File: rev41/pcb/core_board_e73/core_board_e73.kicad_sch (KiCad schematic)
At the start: 17 parts, among them J1 USB_C_Receptacle_USB2.0_16P, J2 Conn_02x10_Odd_Even, J3 Conn_02x10_Odd_Even, J4 USB_C_Receptacle_USB2.0_16P, J5 Conn_01x08_MountingPin, J6 Conn_01x08_MountingPin, J7 Debug, U1 E73-2G4M08S1C, Y1 32.768kHz

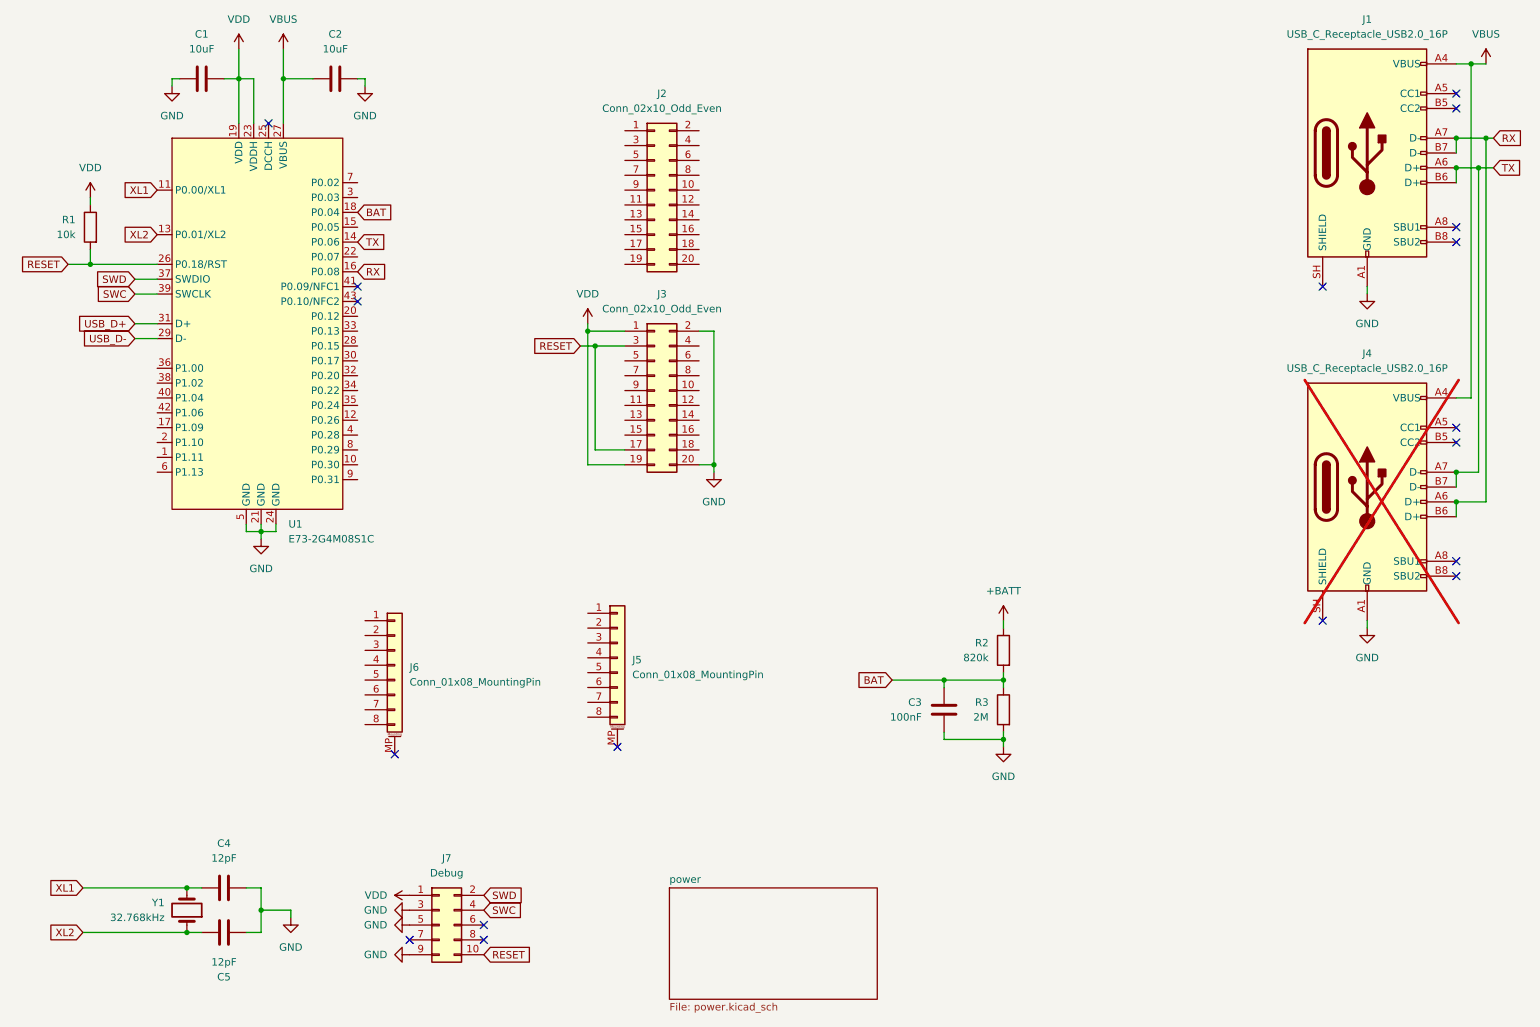
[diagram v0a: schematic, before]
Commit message: feat: core board e73 basic routed
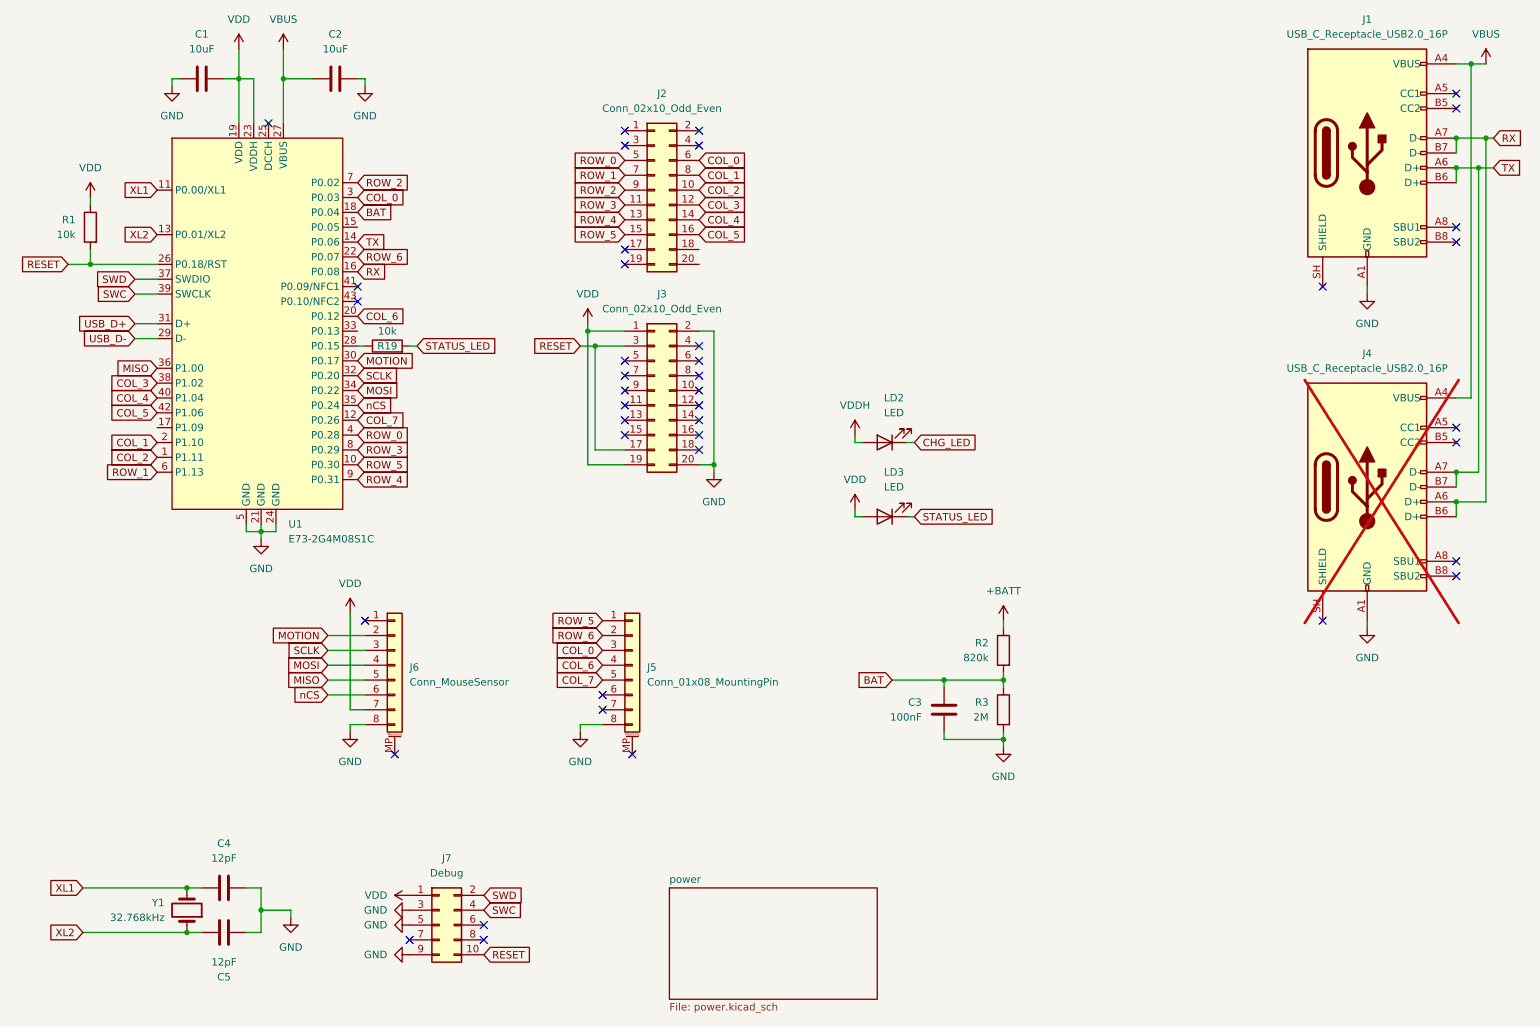
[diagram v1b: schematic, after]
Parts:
- added LD2, LD3: LED, LED_SMD:LED_0603_1608Metric_Pad1.05x0.95mm_HandSolder, symbol Device:LED
- added R19: 10k, Resistor_SMD:R_0402_1005Metric, symbol Device:R
- J6: value Conn_01x08_MountingPin -> Conn_MouseSensor
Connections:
- net GND: now also J5.8 (Pin_8), J6.8 (Pin_8)
- net VDD: now also J6.7 (Pin_7), LD3.2 (A)
- net MOTION: now reaches J6.2 (Pin_2)
- net MOTION: now also U1.30 (P0.17)
- net SCLK: now reaches J6.3 (Pin_3)
- net SCLK: now also U1.32 (P0.20)
- net MOSI: now reaches J6.4 (Pin_4)
- net MOSI: now also U1.34 (P0.22)
- net MISO: now reaches J6.5 (Pin_5)
- net MISO: now also U1.36 (P1.00)
- net nCS: now reaches J6.6 (Pin_6)
- net nCS: now also U1.35 (P0.24)
- net COL_2: now reaches J2.10 (Pin_10)
- net COL_2: now also U1.1 (P1.11)
- net ROW_3: now reaches J2.11 (Pin_11)
- net ROW_3: now also U1.8 (P0.29)
- net COL_3: now reaches J2.12 (Pin_12)
- net COL_3: now also U1.38 (P1.02)
- net ROW_4: now reaches J2.13 (Pin_13)
- net ROW_4: now also U1.9 (P0.31)
- net COL_4: now reaches J2.14 (Pin_14)
- net COL_4: now also U1.40 (P1.04)
- net ROW_5: now reaches J2.15 (Pin_15)
- net ROW_5: now also J5.1 (Pin_1), U1.10 (P0.30)
- net COL_5: now reaches J2.16 (Pin_16)
- net COL_5: now also U1.42 (P1.06)
- net ROW_0: now reaches J2.5 (Pin_5)
- net ROW_0: now also U1.4 (P0.28)
- net COL_0: now reaches J2.6 (Pin_6)
- net COL_0: now also J5.3 (Pin_3), U1.3 (P0.03)
- net ROW_1: now reaches J2.7 (Pin_7)
- net ROW_1: now also U1.6 (P1.13)
- net COL_1: now reaches J2.8 (Pin_8)
- net COL_1: now also U1.2 (P1.10)
- net ROW_2: now reaches J2.9 (Pin_9)
- net ROW_2: now also U1.7 (P0.02)
- net COL_7: now reaches U1.12 (P0.26)
- net COL_7: now also J5.5 (Pin_5)
- net COL_6: now reaches U1.20 (P0.12)
- net COL_6: now also J5.4 (Pin_4)
- net ROW_6: now reaches U1.22 (P0.07)
- net ROW_6: now also J5.2 (Pin_2)
- net at U1.28 (P0.15): now also R19.1
- new net CHG_LED: LD2.1 (K)
- new net STATUS_LED: LD3.1 (K), R19.2
- new net VDDH: LD2.2 (A)
- no-connect marks 18 -> 41
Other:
- moved on the sheet: J5

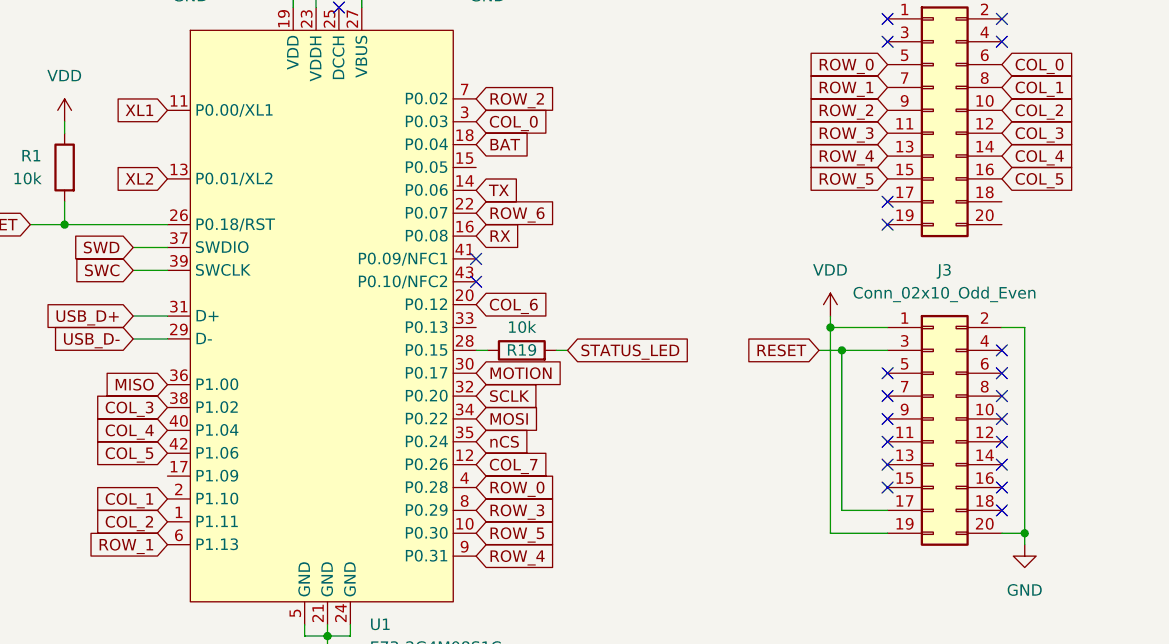
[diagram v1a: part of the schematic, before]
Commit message: feat: update silkscreen
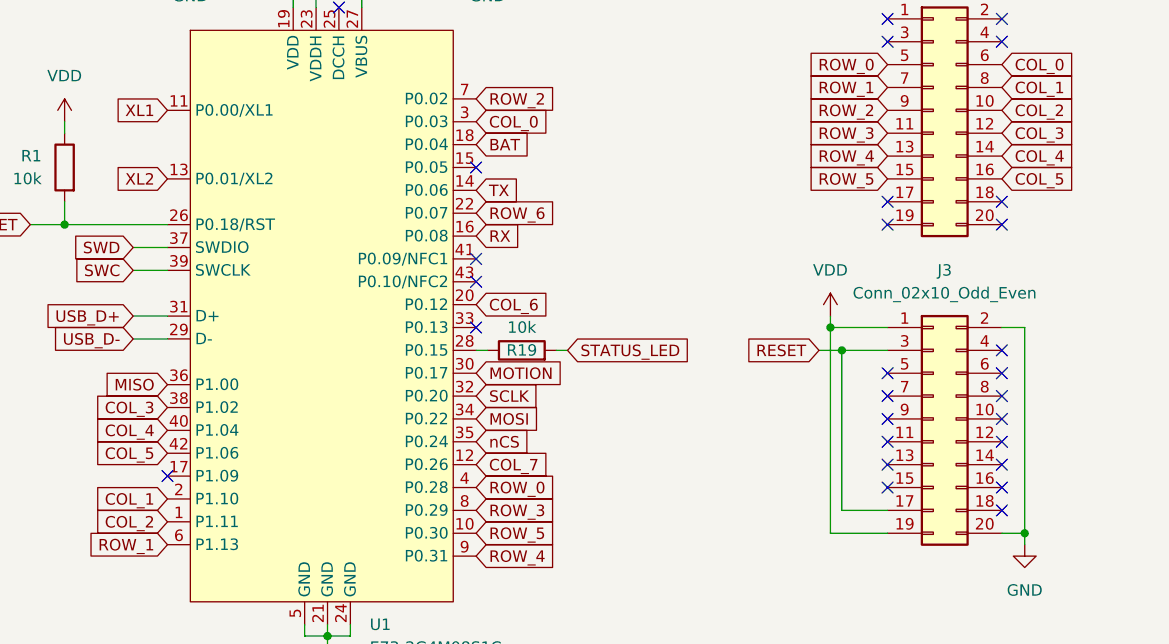
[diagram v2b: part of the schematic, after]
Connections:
- no-connect marks 41 -> 46
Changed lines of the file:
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@@
+	)
+	(no_connect
+		(at 80.01 74.93)
 	)
 	(no_connect
@@
 	)
 	(no_connect
+		(at 138.43 60.96)
+	)
+	(no_connect
 		(at 138.43 82.55)
 	)
@@
 	(no_connect
 		(at 267.97 91.44)
+	)
+	(no_connect
+		(at 80.01 57.15)
 	)
 	(no_connect
@@
 	)
 	(no_connect
+		(at 45.72 91.44)
+	)
+	(no_connect
 		(at 125.73 92.71)
 	)
@@
 	)
 	(no_connect
+		(at 138.43 63.5)
+	)
+	(no_connect

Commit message: feat: update title block
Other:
- company: (none) -> SideraKB
- title: (none) -> ErgoSNM Keyboard - Core Board (E73)
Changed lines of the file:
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@@
 	(generator_version "10.0")
 	(paper "A4")
+	(title_block
+		(title "ErgoSNM Keyboard - Core Board (E73)")
+		(rev "4.1.A")
+		(company "SideraKB")
+		(comment 1 "Open source hardware, CERN-OHL-P_v2")
+		(comment 2 "https://github.com/siderakb/ergo-snm-keyboard")
+	)
 	(junction
 		(at 270.51 29.21)

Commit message: feat: update BOM
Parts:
- C1, C2: JLCPCB Part # (none) -> C19702; MFR. Part # (none) -> CL10A106KP8NNNC
- C3: JLCPCB Part # (none) -> C1525; MFR. Part # (none) -> CL05B104KO5NNNC
- C4, C5: JLCPCB Part # (none) -> C1547; MFR. Part # (none) -> 0402CG120J500NT
- J1, J4: JLCPCB Part # (none) -> C165948; MFR. Part # (none) -> TYPE-C-31-M-12
- J5, J6: JLCPCB Part # (none) -> C2856797; MFR. Part # (none) -> FPC-05F-8PH20
- R1, R19: JLCPCB Part # (none) -> C25744; MFR. Part # (none) -> 0402WGF1002TCE
- R2: JLCPCB Part # (none) -> C2909386; MFR. Part # (none) -> FRC0402F8203TS
- R3: JLCPCB Part # (none) -> C11512; MFR. Part # (none) -> 0402WGF2004TCE
- U1: JLCPCB Part # (none) -> C356849; MFR. Part # (none) -> E73-2G4M08S1C
- Y1: JLCPCB Part # (none) -> C32346; MFR. Part # (none) -> Q13FC13500004
